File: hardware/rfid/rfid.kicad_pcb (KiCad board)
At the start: 2 copper layers, 75 x 50 mm, 34 parts, among them P1 CONN_01X02, P2 COMMS, U1 CR95HF

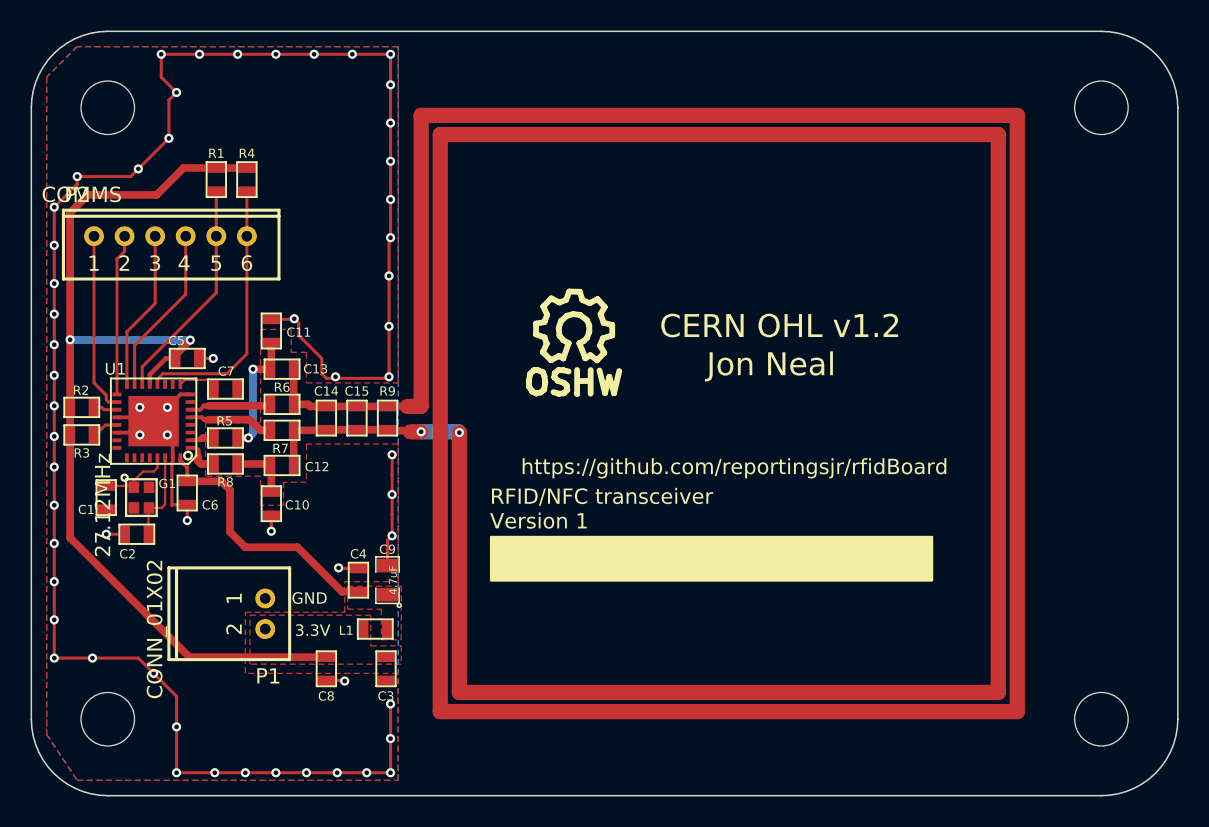
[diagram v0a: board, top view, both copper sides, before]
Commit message: Modify pcb to meet the specs of the voltera PCB printer. Both ground pours were deleted. Vias were deleted and a few of the appropriate size for rivets were added, all traces were bumped up to the minimum reasonable size (0.25mm).
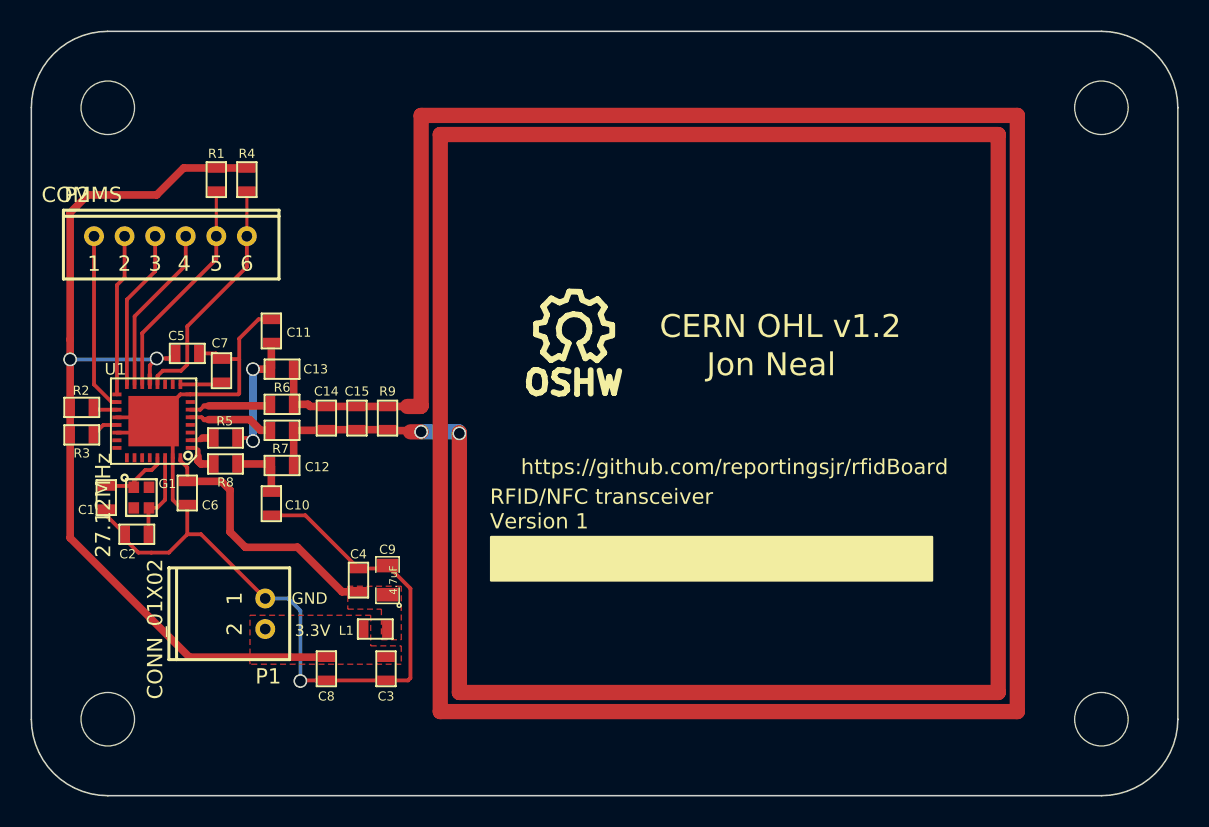
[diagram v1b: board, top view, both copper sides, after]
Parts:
- moved C7 1.23 mm to (168.4, 82.2), turned to 90 degrees
- moved C5 0.33 mm to (166.2, 81.1)
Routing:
- net GND: track 156.7 -> 77.4 mm, vias 61 -> 1
- net 3V3: track 66.3 -> 63.1 mm
- net Net-(P2-Pad6): track 17.5 -> 15.8 mm
- removed copper zone on B.Cu, net GND
- removed copper zone on F.Cu, net GND
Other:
- net class Default removed
